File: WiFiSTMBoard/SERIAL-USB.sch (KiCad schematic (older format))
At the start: 6 parts

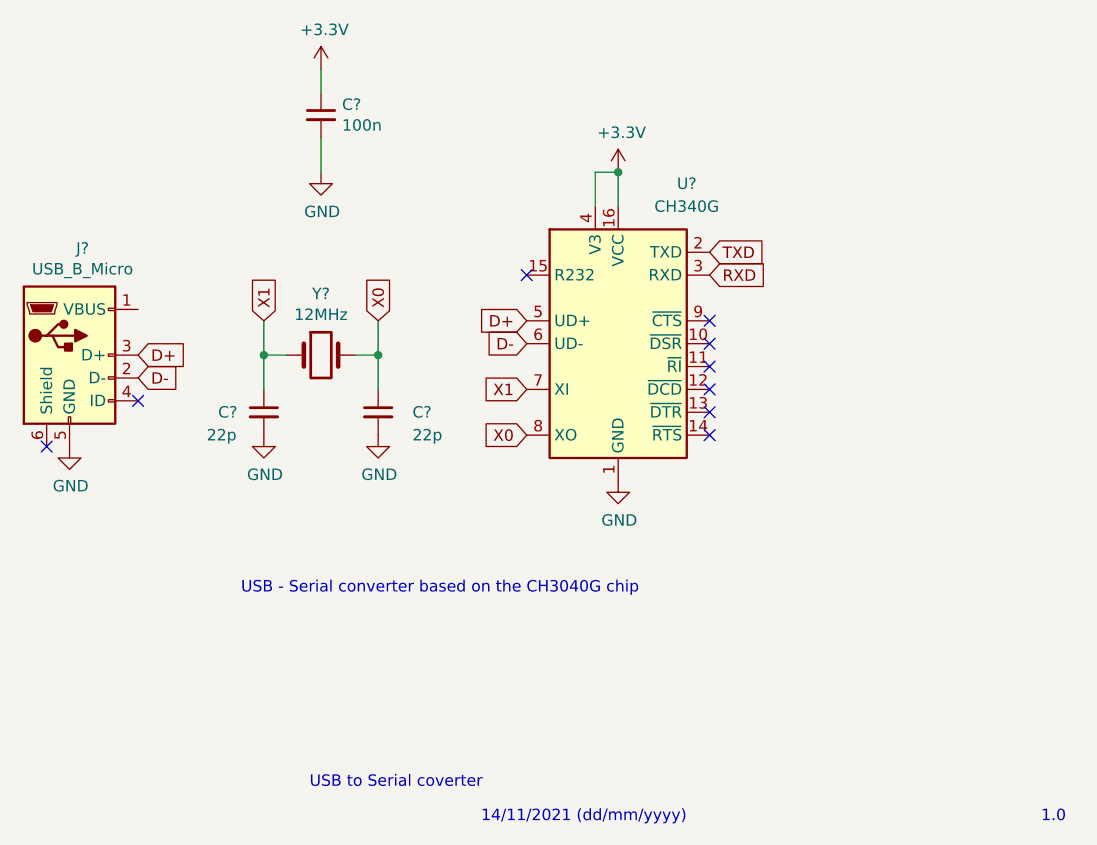
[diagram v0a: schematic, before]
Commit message: finished serial circuit
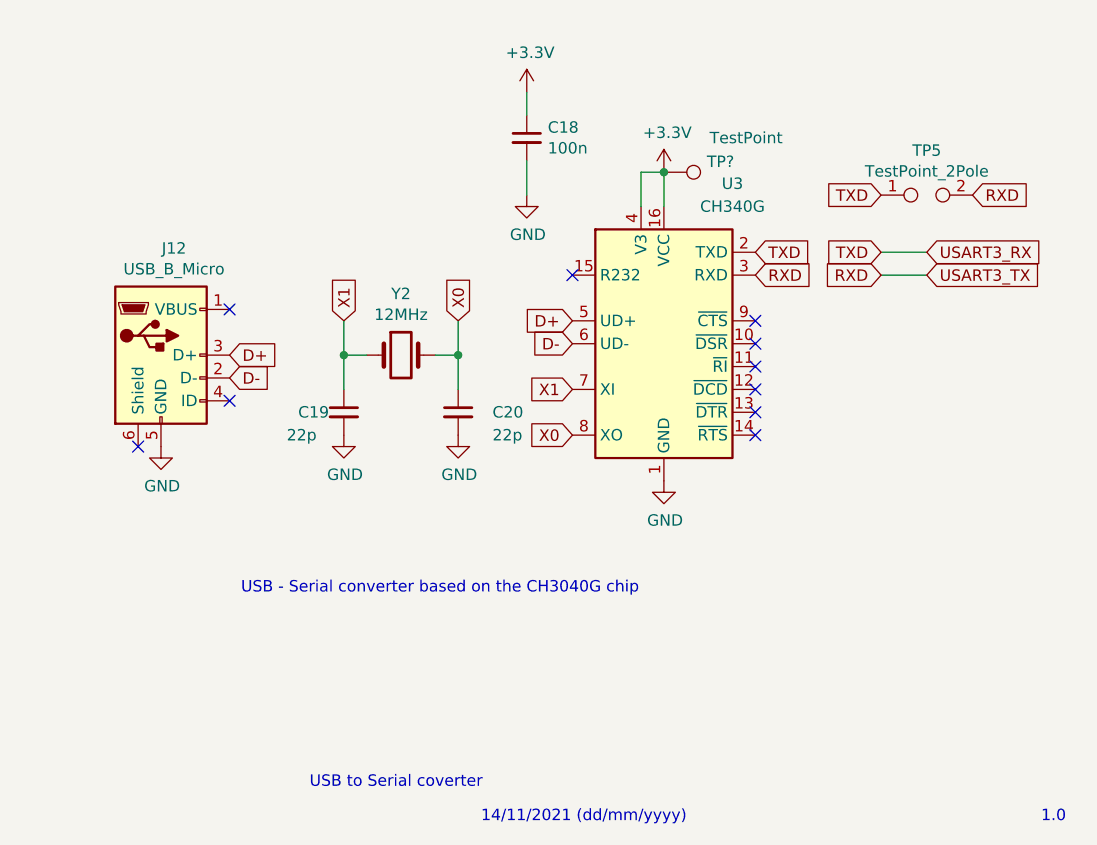
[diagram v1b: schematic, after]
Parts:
- added TP5: TestPoint_2Pole, symbol Connector:TestPoint_2Pole
- added TP?: TestPoint, symbol Connector:TestPoint
- gave numbers to parts that had none: 6
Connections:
- net +3V3: now also TP?.1
- net RXD: now also TP5.2
- net TXD: now also TP5.1
- no-connect marks 9 -> 10
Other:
- moved on the sheet: C18, C19, C20, J12, U3, Y2
